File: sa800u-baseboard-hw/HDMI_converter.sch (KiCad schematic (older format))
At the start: 17 parts, among them U4 LT9611, Y2 ECS-1618-250-BN-TR

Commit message: introducing minor genreal improvements
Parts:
- removed U4: LT9611, symbol HDMI:LT9611
- removed Y2: ECS-1618-250-BN-TR, symbol Oscillators:ECS-1618-250-BN-TR
- added U?: LT9611, antmicro-footprints:LT9611, symbol antmicroInterfaceControllers:LT9611
- added Y?: ECS-1618-250-BN-TR, antmicro-footprints:OSC_ECS-1618-250-BN-TR, symbol antmicroOscillators:ECS-1618-250-BN-TR
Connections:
- net +1V8: now also Y?.1 (TRI-STATE)
- net CEC_GPIO6: now also U?.24 (CEC_GPIO6)
- net DSI1_CLK_N: now also U?.9 (MC_N0)
- net DSI1_CLK_P: now also U?.10 (MC_P0)
- net DSI1_LN0_N: now also U?.13 (M0_N0)
- net DSI1_LN1_N: now also U?.11 (M1_N0)
- net DSI1_LN1_P: now also U?.12 (M1_P0), U?.14 (M0_P0)
- net DSI1_LN2_N: now also U?.7 (M2_N0)
- net DSI1_LN2_P: now also U?.8 (M2_P0)
- net DSI1_LN3_N: now also U?.5 (M3_N0)
- net DSI1_LN3_P: now also U?.6 (M3_P0)
- net GND: now also U?.65 (GND), Y?.2 (GND)
- net HDMIOUT_SCL: now also U?.18 (CSCL_GPIO10)
- net HDMIOUT_SDA: now also U?.19 (CSDA_GPIO11)
- net I2C_ADDR: now also U?.25 (I2C_ADDR)
- net I2S_D0_SPDIF: now also U?.30 (I2S_D0_SPDIF)
- net I2S_MCLK: now also U?.29 (I2S_MCLK_GPIO9)
- net I2S_SCLK: now also U?.28 (I2S_SCLK_GPIO8)
- net I2S_WS: now also U?.27 (I2S_WS_GPIO7)
- net INTO_GPIO5: now also U?.23 (INTIO_GPIO5)
- net LKT9611_VDD12: now also U?.53 (VCC12_SYSPLL), U?.54 (VDD)
- net LT9611VCC12_RX: now also U?.56 (VCC12_MRX23)
- net LT9611_VCC12_RX: now also U?.4 (VCC12_MRX01)
- net LT9611_VCC12_TX: now also U?.44 (VCC12_HTX)
- net LT9611_VCC33_IO: now also U?.26 (VC33_IO), U?.34 (VCC33_IO)
- net LT9611_VCC33_RX: now also U?.3 (VCC33_MRX01), U?.55 (VCC33_MRX23)
- net LT9611_VCC33_TX: now also U?.43 (VCC33_HTX)
- net LT9611_VCC_RX: now also U?.51 (VCC33_BG)
- net LT9611_VDD12: now also U?.15 (VDD1), U?.16 (VDD2), U?.31 (VDD3)
- net RST_N: now also U?.17 (RST_N)
- net SCL_HDMI: now also U?.37 (HTX_DSCL)
- net SDA_HDMI: now also U?.36 (HTX_DSDA)
- net TX_CLKM: now also U?.38 (HTX_C-)
- net TX_CLKP: now also U?.39 (HTX_C+)
- net TX_D0M: now also U?.40 (HTX_D0-)
- net TX_D0P: now also U?.41 (HTX_D0+)
- net TX_D1M: now also U?.45 (HTX_D1-)
- net TX_D1P: now also U?.46 (HTX_D1+)
- net TX_D2M: now also U?.47 (HTX_D2-)
- net TX_D2P: now also U?.48 (HTX_D2+)
- net VCOM: now also U?.42 (VCOM)
- net at R42.1, R43.1: now also U?.35 (HTX_HPD)
- net XTALI: now reaches C33.1, R37.2
- net XTALI: now also U?.49 (XTALI), Y?.3 (OUTPUT)
- net XTALO: now reaches C32.1, R37.1
- net XTALO: now also U?.50 (XTALO), Y?.4 (VDD)
- net at R36.2: now also U?.52 (REXT)
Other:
- note removed: "REMARK: Add components to our repository \n(antmicro-kicad-components)"
- note removed: "Why is this 1M resistor here? \n"
- moved on the sheet: C32, C33, R37
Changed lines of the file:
@@
 Comment4 ""
 $EndDescr
-$Comp
-L HDMI:LT9611 U4
-U 1 1 61A0479A
-P 2250 2250
-F 0 "U4" H 2300 2350 50  0000 L CNN
-F 1 "LT9611" H 2450 2350 50  0000 L CNN
-F 2 "" H 1500 1950 50  0001 C CNN
-F 3 "" H 1500 1950 50  0001 C CNN
-	1    2250 2250
-	1    0    0    -1
-$EndComp
 Wire Wire Line
 	1400 3000 2150 3000
@@
 L power:GND #PWR?
 U 1 1 61A80E9F
-P 3200 1100
+P 9800 4100
 AR Path="/618E716E/61A80E9F" Ref="#PWR?"  Part="1"
 AR Path="/6197686D/61A80E9F" Ref="#PWR0115"  Part="1"
-F 0 "#PWR0115" H 3200 850 50  0001 C CNN
-F 1 "GND" H 3205 927 50  0000 C CNN
-F 2 "" H 3200 1100 50  0001 C CNN
-F 3 "" H 3200 1100 50  0001 C CNN
-	1    3200 1100
-	1    0    0    -1
-$EndComp
-Wire Wire Line
-	3200 950  3200 1100
-Wire Wire Line
-	3650 950  3200 950
+F 0 "#PWR0115" H 9800 3850 50  0001 C CNN
+F 1 "GND" H 9805 3927 50  0000 C CNN
+F 2 "" H 9800 4100 50  0001 C CNN
+F 3 "" H 9800 4100 50  0001 C CNN
+	1    9800 4100
+	1    0    0    -1
+$EndComp
 $Comp
 L power:+1V8 #PWR?
 U 1 1 61A80E97
-P 3200 700
+P 7750 3650
 AR Path="/618E716E/61A80E97" Ref="#PWR?"  Part="1"
 AR Path="/6197686D/61A80E97" Ref="#PWR0116"  Part="1"
-F 0 "#PWR0116" H 3200 550 50  0001 C CNN
-F 1 "+1V8" H 3215 873 50  0000 C CNN
-F 2 "" H 3200 700 50  0001 C CNN
-F 3 "" H 3200 700 50  0001 C CNN
-	1    3200 700
-	1    0    0    -1
-$EndComp
-Wire Wire Line
-	3200 850  3200 700
-Wire Wire Line
-	3650 850  3200 850
-$Comp
-L Oscillators:ECS-1618-250-BN-TR Y?
-U 1 1 61A80E8F
-P 3750 750
-AR Path="/618E716E/61A80E8F" Ref="Y?"  Part="1"
-AR Path="/6197686D/61A80E8F" Ref="Y2"  Part="1"
-F 0 "Y2" H 4000 915 50  0000 C CNN
-F 1 "ECS-1618-250-BN-TR" H 4000 824 50  0000 C CNN
-F 2 "" H 3950 800 50  0001 C CNN
-F 3 "" H 3950 800 50  0001 C CNN
-	1    3750 750
-	1    0    0    -1
-$EndComp
-Wire Wire Line
-	4350 950  4600 950
-Wire Wire Line
-	4600 950  4600 1050
-$Comp
-L antmicroCapacitors0402:C_10p_0402 C?
-U 1 1 61A80EAA
-P 4600 1250
-AR Path="/618E716E/61A80EAA" Ref="C?"  Part="1"
-AR Path="/6197686D/61A80EAA" Ref="C32"  Part="1"
-F 0 "C32" H 4715 1295 60  0000 L CNN
-F 1 "C_10p_0402" H 4600 1100 60  0001 C CNN
-F 2 "antmicro-footprints:0402-cap" H 4800 1450 60  0001 L CNN
-F 3 "" H 4600 1250 50  0001 C CNN
-F 4 "MULTICOMP" H 4800 1650 60  0001 L CNN "Manufacturer"
-F 5 "MC0402N100D500CT" H 4800 1550 60  0001 L CNN "MPN"
-F 6 "10p" H 4715 1197 50  0000 L CNN "Val"
-	1    4600 1250
-	1    0    0    -1
-$EndComp
-$Comp
-L power:GND #PWR?
-U 1 1 61A80EB0
-P 4600 1400
-AR Path="/618E716E/61A80EB0" Ref="#PWR?"  Part="1"
-AR Path="/6197686D/61A80EB0" Ref="#PWR0117"  Part="1"
-F 0 "#PWR0117" H 4600 1150 50  0001 C CNN
-F 1 "GND" H 4605 1227 50  0000 C CNN
-F 2 "" H 4600 1400 50  0001 C CNN
-F 3 "" H 4600 1400 50  0001 C CNN
-	1    4600 1400
-	1    0    0    -1
-$EndComp
-Wire Wire Line
-	4350 850  5150 850
-Wire Wire Line
-	5150 850  5150 1050
-$Comp
-L antmicroCapacitors0402:C_10p_0402 C?
-U 1 1 61A80EBB
-P 5150 1250
-AR Path="/618E716E/61A80EBB" Ref="C?"  Part="1"
-AR Path="/6197686D/61A80EBB" Ref="C33"  Part="1"
-F 0 "C33" H 5265 1295 60  0000 L CNN
-F 1 "C_10p_0402" H 5150 1100 60  0001 C CNN
-F 2 "antmicro-footprints:0402-cap" H 5350 1450 60  0001 L CNN
-F 3 "" H 5150 1250 50  0001 C CNN
-F 4 "MULTICOMP" H 5350 1650 60  0001 L CNN "Manufacturer"
-F 5 "MC0402N100D500CT" H 5350 1550 60  0001 L CNN "MPN"
-F 6 "10p" H 5265 1197 50  0000 L CNN "Val"
-	1    5150 1250
-	1    0    0    -1
-$EndComp
-$Comp
-L power:GND #PWR?
-U 1 1 61A80EC1
-P 5150 1400
-AR Path="/618E716E/61A80EC1" Ref="#PWR?"  Part="1"
-AR Path="/6197686D/61A80EC1" Ref="#PWR0118"  Part="1"
-F 0 "#PWR0118" H 5150 1150 50  0001 C CNN
-F 1 "GND" H 5155 1227 50  0000 C CNN
-F 2 "" H 5150 1400 50  0001 C CNN
-F 3 "" H 5150 1400 50  0001 C CNN
-	1    5150 1400
-	1    0    0    -1
-$EndComp
-Connection ~ 4600 1050
-Wire Wire Line
-	4600 1050 4600 1100
-$Comp
-L antmicroResistors0402:R_1M0_0402 R?
-U 1 1 61A80ECC
-P 4900 1050
-AR Path="/618E716E/61A80ECC" Ref="R?"  Part="1"
-AR Path="/6197686D/61A80ECC" Ref="R37"  Part="1"
-F 0 "R37" H 4900 1263 60  0000 C CNN
-F 1 "R_1M0_0402" H 4900 900 60  0001 C CNN
-F 2 "antmicro-footprints:0402-res" H 5100 1250 60  0001 L CNN
-F 3 "" H 4900 1050 50  0001 C CNN
-F 4 "TE CONNECTIVITY" H 5100 1450 60  0001 L CNN "Manufacturer"
-F 5 "CRG0402F1M0" H 5100 1350 60  0001 L CNN "MPN"
-F 6 "1M0" H 4900 1165 50  0000 C CNN "Val"
-	1    4900 1050
-	1    0    0    -1
-$EndComp
-Wire Wire Line
-	4600 1050 4750 1050
-Wire Wire Line
-	5050 1050 5150 1050
-Connection ~ 5150 1050
-Wire Wire Line
-	5150 1050 5150 1100
-Text Notes 4600 750  0    50   ~ 0
-Why is this 1M resistor here? \n
-Wire Wire Line
-	4600 1050 4300 1050
-Wire Wire Line
-	4300 1050 4300 2150
-Wire Wire Line
-	5150 1050 5600 1050
-Wire Wire Line
-	5600 1050 5600 2150
-Wire Wire Line
-	5600 2150 4400 2150
+F 0 "#PWR0116" H 7750 3500 50  0001 C CNN
+F 1 "+1V8" H 7765 3823 50  0000 C CNN
+F 2 "" H 7750 3650 50  0001 C CNN
+F 3 "" H 7750 3650 50  0001 C CNN
+	1    7750 3650
+	1    0    0    -1
+$EndComp
+Wire Wire Line
+	7750 3800 7750 3650
+Wire Wire Line
+	8200 3800 7750 3800
 Text GLabel 1400 3000 0    50   Input ~ 0
 LT9611_VCC33_RX
@@
 Text GLabel 4200 7050 3    50   Input ~ 0
 LT9611_VDD12
-Text Notes 525  2275 0    50   ~ 0
-REMARK: Add components to our repository \n(antmicro-kicad-components)
+$Comp
+L antmicroInterfaceControllers:LT9611 U?
+U 1 1 61A27AED
+P 2250 2250
+F 0 "U?" H 4994 1087 50  0000 L CNN
+F 1 "LT9611" H 4994 996 50  0000 L CNN
+F 2 "antmicro-footprints:LT9611" H 2250 2250 50  0001 C CNN
+F 3 "https://dev.antmicro.com/attachments/145681/LT9611_Datasheet_R2.0%20(1).pdf" H 2250 2250 50  0001 C CNN
+F 4 "LT9611" H 4994 905 50  0000 L CNN "MPN"
+F 5 "LONTIUM" H 4994 814 50  0000 L CNN "Manufacturer"
+	1    2250 2250
+	1    0    0    -1
+$EndComp
+$Comp
+L antmicroOscillators:ECS-1618-250-BN-TR Y?
+U 1 1 61A99388
+P 8400 3400
+F 0 "Y?" H 9000 3749 50  0000 C CNN
+F 1 "ECS-1618-250-BN-TR" H 9000 3658 50  0000 C CNN
+F 2 "antmicro-footprints:OSC_ECS-1618-250-BN-TR" H 8400 3400 50  0001 C CNN
+F 3 "https://ecsxtal.com/store/pdf/ECS_1618.pdf" H 8400 3400 50  0001 C CNN
+F 4 "ECS-1618-250-BN-TR" H 9000 3567 50  0000 C CNN "MPN"
+F 5 "ECSXTAL" H 9000 3476 50  0000 C CNN "Manufacturer"
+	1    8400 3400
+	1    0    0    -1
+$EndComp
+Wire Wire Line
+	9200 4700 9200 4750
+Connection ~ 9200 4700
+Wire Wire Line
+	9100 4700 9200 4700
+Wire Wire Line
+	8650 4700 8800 4700
+$Comp
+L antmicroResistors0402:R_1M0_0402 R?
+U 1 1 61A80ECC
+P 8950 4700
+AR Path="/618E716E/61A80ECC" Ref="R?"  Part="1"
+AR Path="/6197686D/61A80ECC" Ref="R37"  Part="1"
+F 0 "R37" H 8950 4913 60  0000 C CNN
+F 1 "R_1M0_0402" H 8950 4550 60  0001 C CNN
+F 2 "antmicro-footprints:0402-res" H 9150 4900 60  0001 L CNN
+F 3 "" H 8950 4700 50  0001 C CNN
+F 4 "TE CONNECTIVITY" H 9150 5100 60  0001 L CNN "Manufacturer"
+F 5 "CRG0402F1M0" H 9150 5000 60  0001 L CNN "MPN"
+F 6 "1M0" H 8950 4815 50  0000 C CNN "Val"
+	1    8950 4700
+	1    0    0    -1
+$EndComp
+Wire Wire Line
+	8650 4700 8650 4750
+Connection ~ 8650 4700
+$Comp
+L power:GND #PWR?
+U 1 1 61A80EC1
+P 9200 5050
+AR Path="/618E716E/61A80EC1" Ref="#PWR?"  Part="1"
+AR Path="/6197686D/61A80EC1" Ref="#PWR0118"  Part="1"
+F 0 "#PWR0118" H 9200 4800 50  0001 C CNN
+F 1 "GND" H 9205 4877 50  0000 C CNN
+F 2 "" H 9200 5050 50  0001 C CNN
+F 3 "" H 9200 5050 50  0001 C CNN
+	1    9200 5050
+	1    0    0    -1
+$EndComp
+$Comp
+L antmicroCapacitors0402:C_10p_0402 C?
+U 1 1 61A80EBB
+P 9200 4900
+AR Path="/618E716E/61A80EBB" Ref="C?"  Part="1"
+AR Path="/6197686D/61A80EBB" Ref="C33"  Part="1"
+F 0 "C33" H 9315 4945 60  0000 L CNN
+F 1 "C_10p_0402" H 9200 4750 60  0001 C CNN
+F 2 "antmicro-footprints:0402-cap" H 9400 5100 60  0001 L CNN
+F 3 "" H 9200 4900 50  0001 C CNN
+F 4 "MULTICOMP" H 9400 5300 60  0001 L CNN "Manufacturer"
+F 5 "MC0402N100D500CT" H 9400 5200 60  0001 L CNN "MPN"
+F 6 "10p" H 9315 4847 50  0000 L CNN "Val"
+	1    9200 4900
+	1    0    0    -1
+$EndComp
+Wire Wire Line
+	9200 4500 9200 4700
+$Comp
+L power:GND #PWR?
+U 1 1 61A80EB0
+P 8650 5050
+AR Path="/618E716E/61A80EB0" Ref="#PWR?"  Part="1"
+AR Path="/6197686D/61A80EB0" Ref="#PWR0117"  Part="1"
+F 0 "#PWR0117" H 8650 4800 50  0001 C CNN
+F 1 "GND" H 8655 4877 50  0000 C CNN
+F 2 "" H 8650 5050 50  0001 C CNN
+F 3 "" H 8650 5050 50  0001 C CNN
+	1    8650 5050
+	1    0    0    -1
+$EndComp
+$Comp
+L antmicroCapacitors0402:C_10p_0402 C?
+U 1 1 61A80EAA
+P 8650 4900
+AR Path="/618E716E/61A80EAA" Ref="C?"  Part="1"
+AR Path="/6197686D/61A80EAA" Ref="C32"  Part="1"
+F 0 "C32" H 8765 4945 60  0000 L CNN
+F 1 "C_10p_0402" H 8650 4750 60  0001 C CNN
+F 2 "antmicro-footprints:0402-cap" H 8850 5100 60  0001 L CNN
+F 3 "" H 8650 4900 50  0001 C CNN
+F 4 "MULTICOMP" H 8850 5300 60  0001 L CNN "Manufacturer"
+F 5 "MC0402N100D500CT" H 8850 5200 60  0001 L CNN "MPN"
+F 6 "10p" H 8765 4847 50  0000 L CNN "Val"
+	1    8650 4900
+	1    0    0    -1
+$EndComp
+Wire Wire Line
+	8200 3600 7850 3600
+Wire Wire Line
+	7850 3600 7850 4700
+Wire Wire Line
+	7850 4700 8650 4700
+Wire Wire Line
+	9800 3600 10200 3600
+Wire Wire Line
+	10200 3600 10200 4700
+Wire Wire Line
+	9200 4700 10200 4700
+Wire Wire Line
+	8650 4500 8650 4700
+Wire Wire Line
+	9800 4000 9800 4100
+Text Label 4300 1250 1    50   ~ 0
+XTALO
+Text Label 4400 1250 1    50   ~ 0
+XTALI
+Wire Wire Line
+	4300 1250 4300 2150
+Wire Wire Line
+	4400 1250 4400 2150
+Text Label 8650 4500 1    50   ~ 0
+XTALO
+Text Label 9200 4500 1    50   ~ 0
+XTALI
 $EndSCHEMATC

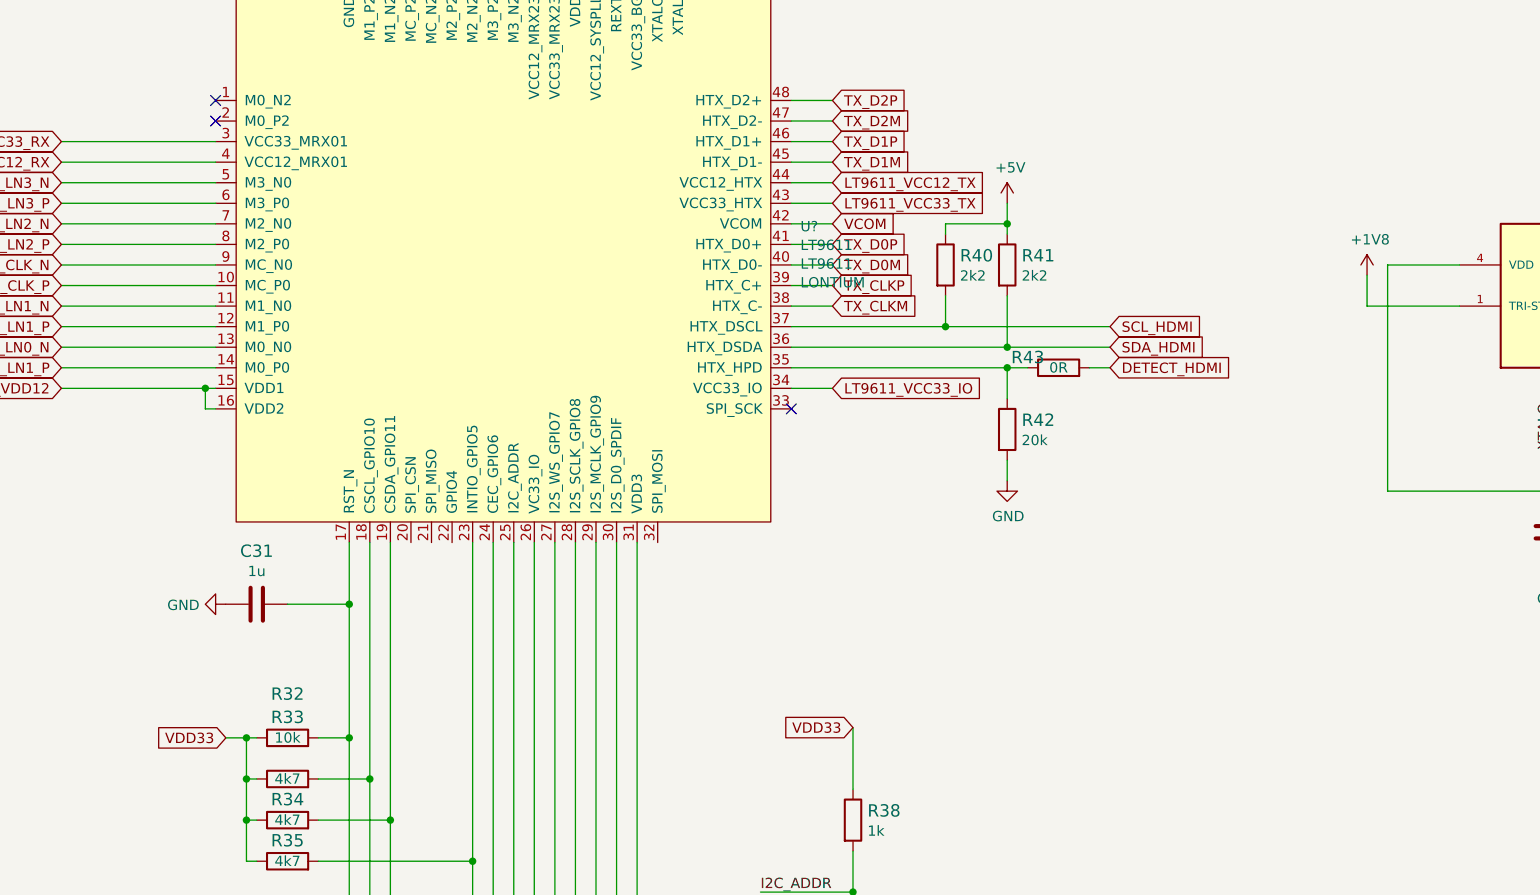
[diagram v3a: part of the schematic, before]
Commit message: fixed / unified power labels
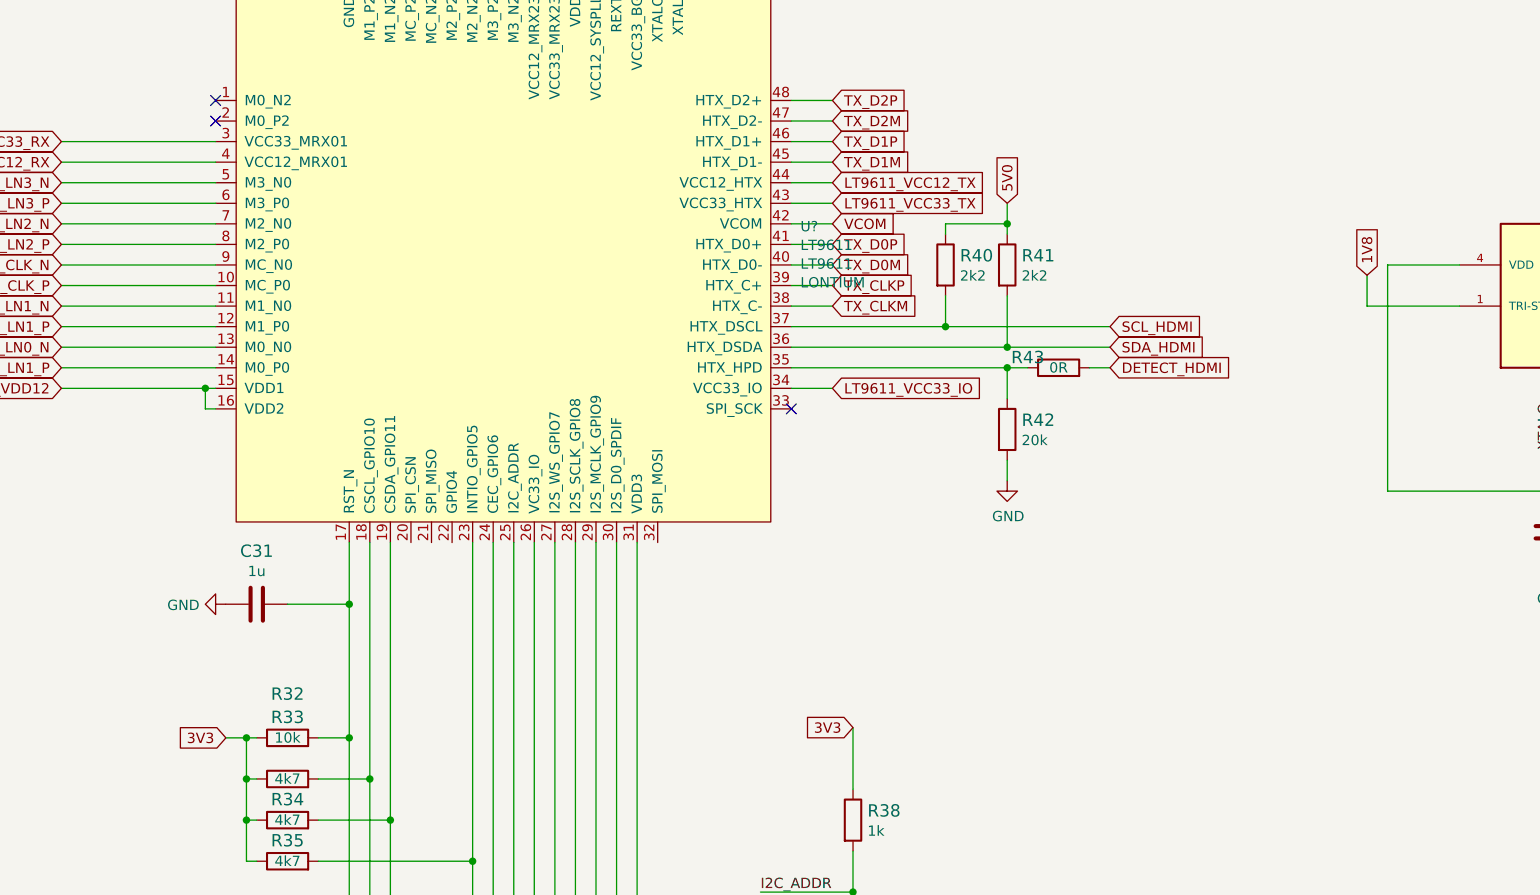
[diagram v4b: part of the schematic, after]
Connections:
- net +1V8 renamed 1V8
- net +5V renamed 5V0
- net VDD33 renamed 3V3
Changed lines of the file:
@@
 $EndComp
 Text GLabel 2200 5900 0    50   Input ~ 0
-VDD33
+3V3
 $Comp
 L antmicroResistors0603:R_10k_0603 R32
@@
 	4200 4950 4200 7050
 Text GLabel 5250 5850 0    50   Input ~ 0
-VDD33
+3V3
 Wire Wire Line
 	5250 5850 5250 6150
@@
 Connection ~ 6000 3400
 $Comp
-L power:+5V #PWR0106
-U 1 1 61A3A044
-P 6000 3300
-F 0 "#PWR0106" H 6000 3150 50  0001 C CNN
-F 1 "+5V" H 6015 3473 50  0000 C CNN
-F 2 "" H 6000 3300 50  0001 C CNN
-F 3 "" H 6000 3300 50  0001 C CNN
-	1    6000 3300
-	1    0    0    -1
-$EndComp
-$Comp
 L antmicroResistors0402:R_0R_0402 R43
 U 1 1 61A3ACDD
@@
 F 3 "" H 9800 4100 50  0001 C CNN
 	1    9800 4100
-	1    0    0    -1
-$EndComp
-$Comp
-L power:+1V8 #PWR?
-U 1 1 61A80E97
-P 7750 3650
-AR Path="/618E716E/61A80E97" Ref="#PWR?"  Part="1"
-AR Path="/6197686D/61A80E97" Ref="#PWR0116"  Part="1"
-F 0 "#PWR0116" H 7750 3500 50  0001 C CNN
-F 1 "+1V8" H 7765 3823 50  0000 C CNN
-F 2 "" H 7750 3650 50  0001 C CNN
-F 3 "" H 7750 3650 50  0001 C CNN
-	1    7750 3650
 	1    0    0    -1
 $EndComp
@@
 Text Label 9200 4500 1    50   ~ 0
 XTALI
+Text GLabel 6000 3300 1    50   Input ~ 0
+5V0
+Text GLabel 7750 3650 1    50   Input ~ 0
+1V8
 $EndSCHEMATC
